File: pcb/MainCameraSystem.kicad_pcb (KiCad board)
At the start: 4 copper layers, 50 x 50 mm, 5 parts, among them J1 OV5640 Ribbon Connector, J2 ST-Link, J3 Micro_SD_Card, U1 STM32H533VET6

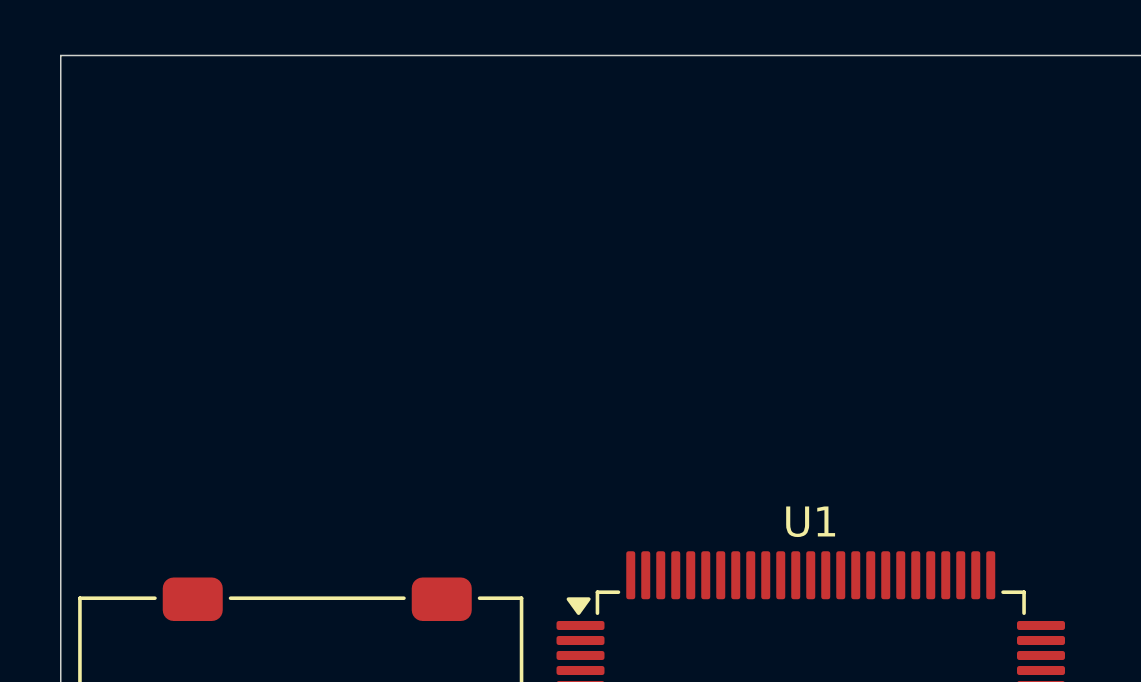
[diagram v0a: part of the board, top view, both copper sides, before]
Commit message: Integrated UART Bridge onto Camera PCB
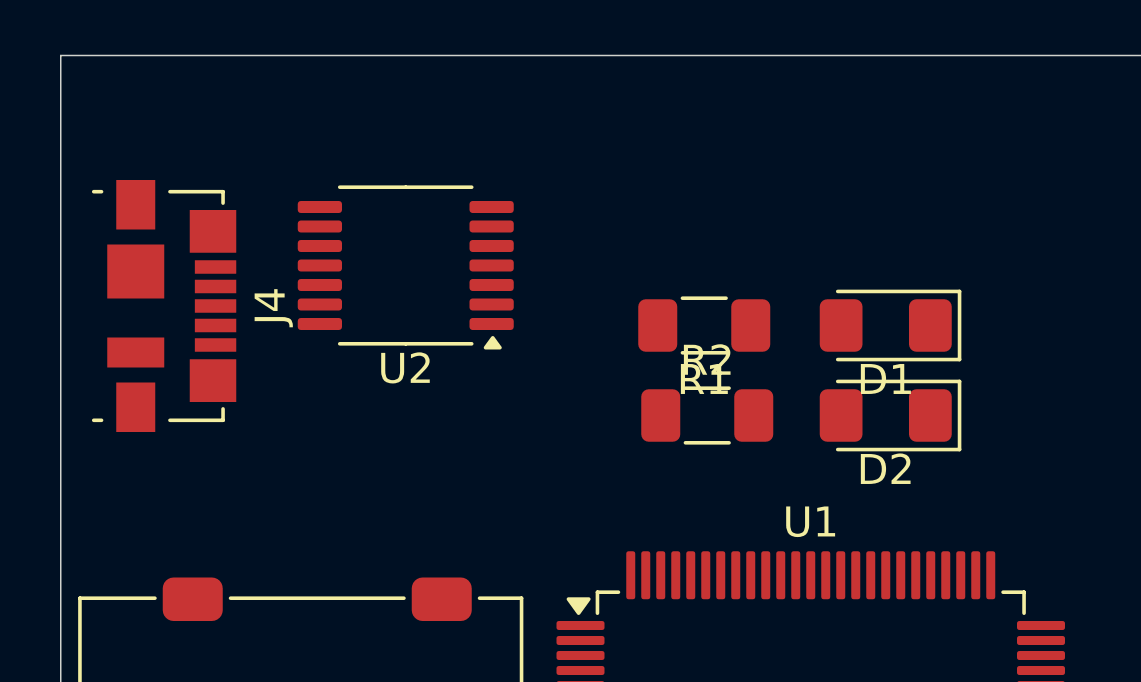
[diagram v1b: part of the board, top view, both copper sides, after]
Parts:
- added D1: GREEN, LED_SMD:LED_1206_3216Metric_Pad1.42x1.75mm_HandSolder, F.Cu at (152.5, 84.0)
- added D2: RED, LED_SMD:LED_1206_3216Metric_Pad1.42x1.75mm_HandSolder, F.Cu at (152.5, 87.0)
- added J4: USB_B_Micro, Connector_USB:USB_Micro-B_Molex_47346-0001, F.Cu at (128.7, 83.3)
- added R1: 2K, Resistor_SMD:R_1206_3216Metric_Pad1.30x1.75mm_HandSolder, F.Cu at (146.4, 84.0)
- added R2: 2K, Resistor_SMD:R_1206_3216Metric_Pad1.30x1.75mm_HandSolder, F.Cu at (146.6, 87.0)
- added U2: MCP2221AxST, Package_SO:TSSOP-14_4.4x5mm_P0.65mm, F.Cu at (136.5, 82.0)

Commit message: Emptied out schematic and layout of `MainCameraSystem`.
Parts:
- removed D1: GREEN, LED_SMD:LED_1206_3216Metric_Pad1.42x1.75mm_HandSolder
- removed D2: RED, LED_SMD:LED_1206_3216Metric_Pad1.42x1.75mm_HandSolder
- removed J1: OV5640 Ribbon Connector, pcb:Flat Flexible Cable 24-Pin 0.5mm Connector
- removed J2: ST-Link, Connector_IDC:IDC-Header_2x05_P2.54mm_Horizontal
- removed J3: Micro_SD_Card, pcb:microSD_HC_Molex_47219-2001
- removed J4: USB_B_Micro, Connector_USB:USB_Micro-B_Molex_47346-0001
- removed N1: Housing, pcb:MainCameraSystemHousing
- removed R1, R2: 2K, Resistor_SMD:R_1206_3216Metric_Pad1.30x1.75mm_HandSolder
- removed U1: STM32H533VET6, Package_QFP:LQFP-100_14x14mm_P0.5mm
- removed U2: MCP2221AxST, Package_SO:TSSOP-14_4.4x5mm_P0.65mm
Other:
- board outline removed

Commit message: Most of the essential components slapped together for `MainCameraSystem`.
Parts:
- added D5: 150141M173100, LED_SMD:LED_RGB_Wuerth-PLCC4_3.2x2.8mm_150141M173100, F.Cu at (133.0, 90.0)
- added H1: MountingHole, MountingHole:MountingHole_3.2mm_M3, F.Cu at (134.0, 84.0)
- added H2: MountingHole, MountingHole:MountingHole_3.2mm_M3, F.Cu at (166.0, 84.0)
- added H3: MountingHole, MountingHole:MountingHole_3.2mm_M3, F.Cu at (134.0, 116.0)
- added H4: MountingHole, MountingHole:MountingHole_3.2mm_M3, F.Cu at (166.0, 116.0)
- added J1: 0472192001, pcb:microSD_HC_Molex_47219-2001, B.Cu at (150.0, 88.0)
- added J2: Debug, pcb:Molex_PicoBlade_53047-1010_1x10_P1.25mm_Vertical, F.Cu at (131.5, 94.4)
- added J6: FFC2B28-24-G, pcb:Flat Flexible Cable 24-Pin 0.5mm Connector, F.Cu at (149.2, 117.0)
- added SW1: B3U-1000P, Button_Switch_SMD:SW_SPST_B3U-1000P, F.Cu at (133.0, 110.0)
- added SW1: B3U-1000P, Button_Switch_SMD:SW_SPST_B3U-1000P, F.Cu at (136.0, 100.0)
- added U1: STM32H533VET6, Package_QFP:LQFP-100_14x14mm_P0.5mm, F.Cu at (150.0, 100.0)
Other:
- board outline added: 40 x 40 mm

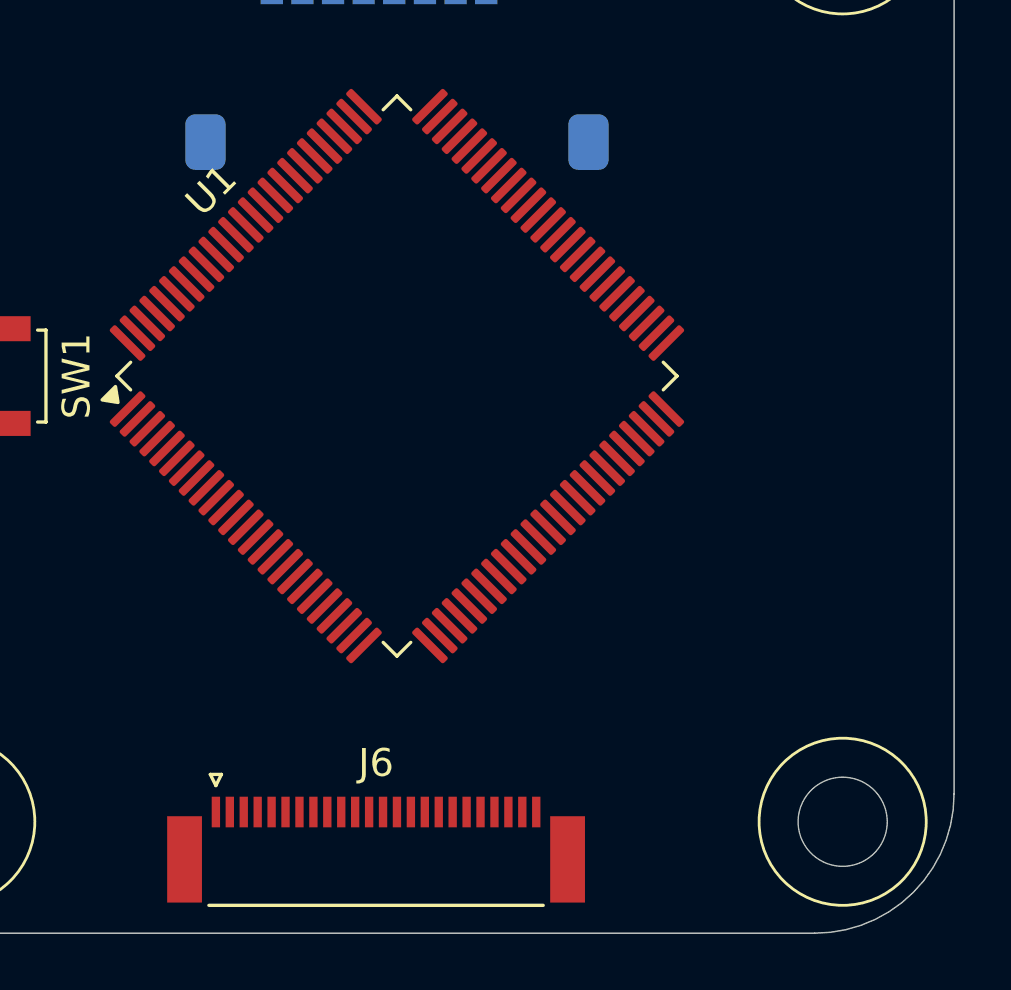
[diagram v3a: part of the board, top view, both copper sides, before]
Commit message: Moved ribbon cable for `MainCameraSystem` per Devon's request.
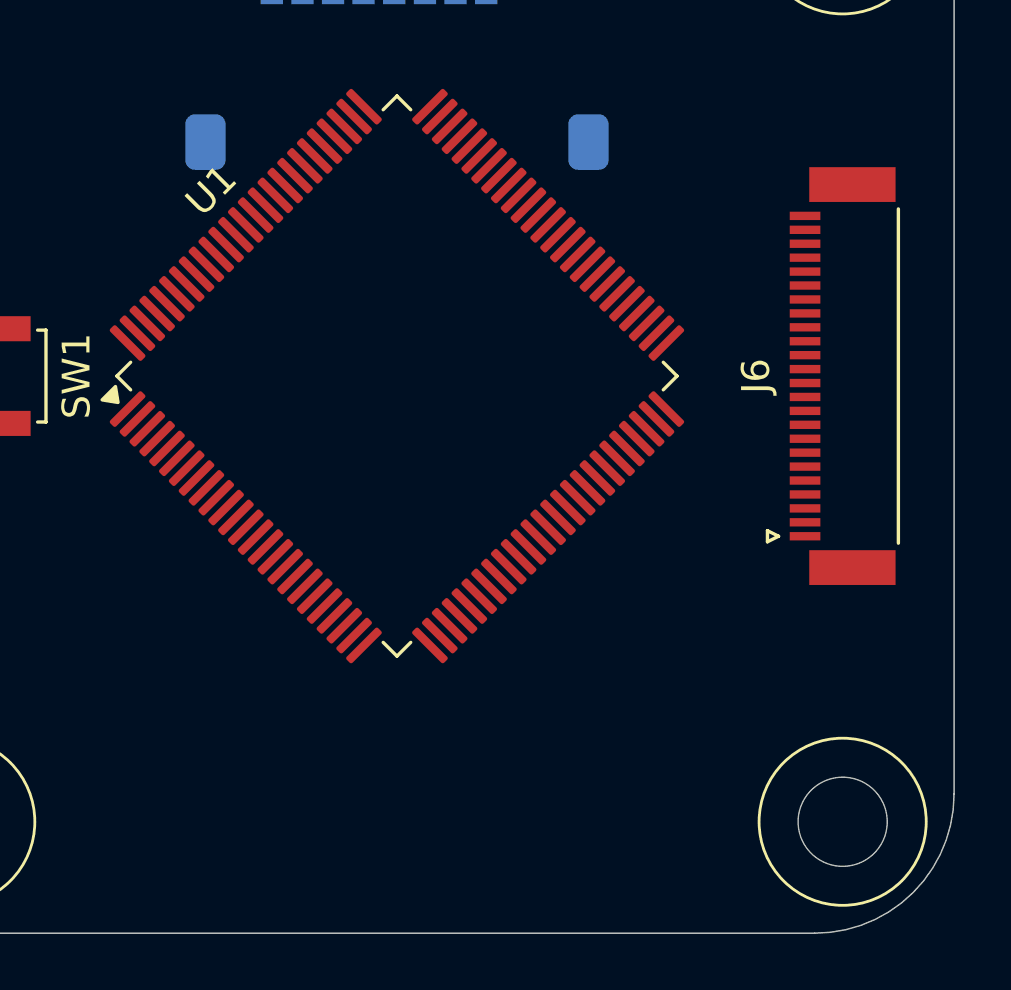
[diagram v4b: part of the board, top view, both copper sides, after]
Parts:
- moved J6 23.9 mm to (166.0, 100.0), turned to 90 degrees
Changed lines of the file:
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@@
 	(footprint "pcb:Flat Flexible Cable 24-Pin 0.5mm Connector"
 		(layer "F.Cu")
-		(at 149.25 117)
+		(at 166 100 90)
 		(descr "FFC/FPC connector, 24 top-side contacts, 0.5mm pitch, SMT")
 		(property "Reference" "J6"
-			(at 0 -3.11 0)
+			(at 0 -3.11 90)
 			(layer "F.SilkS")
 			(effects
@@
 		)
 		(property "Value" "FFC2B28-24-G"
-			(at 0 4.950001 0)
+			(at 0 4.950001 90)
 			(layer "F.Fab")
 			(hide yes)
@@
 		)
 		(property "Datasheet" "~"
-			(at 0 0 0)
+			(at 0 0 90)
 			(layer "F.Fab")
 			(hide yes)
@@
 		)
 		(property "Description" "Generic connector, single row, 01x24, script generated (kicad-library-utils/schlib/autogen/connector/)"
-			(at 0 0 0)
+			(at 0 0 90)
 			(layer "F.Fab")
 			(hide yes)
@@
 		)
 		(property "DigiKey" "https://www.digikey.com/en/products/detail/gct/FFC2B28-24-G/10656928"
-			(at 0 0 0)
+			(at 0 0 90)
 			(layer "F.SilkS")
 			(hide yes)
@@
 		(attr smd)
 		(fp_line
+			(start -5.55 -2.7)
+			(end -5.95 -2.7)
+			(stroke
+				(width 0.12)
+				(type solid)
+			)
+			(layer "F.SilkS")
+		)
+		(fp_line
+			(start -5.95 -2.7)
+			(end -5.75 -2.300001)
+			(stroke
+				(width 0.12)
+				(type solid)
+			)
+			(layer "F.SilkS")
+		)
+		(fp_line
+			(start -5.75 -2.300001)
+			(end -5.55 -2.7)
+			(stroke
+				(width 0.12)
+				(type solid)
+			)
+			(layer "F.SilkS")
+		)
+		(fp_line
 			(start -6 2)
 			(end 6 2)
@@
 			(layer "F.SilkS")
 		)
-		(fp_line
-			(start -5.95 -2.7)
-			(end -5.75 -2.300001)
-			(stroke
-				(width 0.12)
-				(type solid)
-			)
-			(layer "F.SilkS")
-		)
-		(fp_line
-			(start -5.75 -2.300001)
-			(end -5.55 -2.7)
-			(stroke
-				(width 0.12)
-				(type solid)
-			)
-			(layer "F.SilkS")
-		)
-		(fp_line
-			(start -5.55 -2.7)
-			(end -5.95 -2.7)
-			(stroke
-				(width 0.12)
-				(type solid)
-			)
-			(layer "F.SilkS")
-		)
 		(pad "" smd rect
-			(at -6.875 0.349999)
+			(at -6.875 0.349999 90)
 			(size 1.25 3.1)
 			(layers "F.Cu" "F.Mask" "F.Paste")
 		)
 		(pad "" smd rect
-			(at 6.875 0.349999)
+			(at 6.875 0.349999 90)
 			(size 1.25 3.1)
 			(layers "F.Cu" "F.Mask" "F.Paste")
 		)
 		(pad "1" smd rect
-			(at -5.75 -1.35)
+			(at -5.75 -1.35 90)
 			(size 0.3 1.1)
 			(layers "F.Cu" "F.Mask" "F.Paste")
@@
 		)
 		(pad "2" smd rect
-			(at -5.25 -1.35)
+			(at -5.25 -1.35 90)
 			(size 0.3 1.1)
 			(layers "F.Cu" "F.Mask" "F.Paste")
@@
 		)
 		(pad "3" smd rect
-			(at -4.75 -1.35)
+			(at -4.75 -1.35 90)
 			(size 0.3 1.1)
 			(layers "F.Cu" "F.Mask" "F.Paste")
@@
 		)
 		(pad "4" smd rect
-			(at -4.25 -1.35)
+			(at -4.25 -1.35 90)
 			(size 0.3 1.1)
 			(layers "F.Cu" "F.Mask" "F.Paste")
@@
 		)
 		(pad "5" smd rect
-			(at -3.75 -1.35)
+			(at -3.75 -1.35 90)
 			(size 0.3 1.1)
 			(layers "F.Cu" "F.Mask" "F.Paste")
@@
 		)
 		(pad "6" smd rect
-			(at -3.25 -1.35)
+			(at -3.25 -1.35 90)
 			(size 0.3 1.1)
 			(layers "F.Cu" "F.Mask" "F.Paste")
@@
 		)
 		(pad "7" smd rect
-			(at -2.75 -1.35)
+			(at -2.75 -1.35 90)
 			(size 0.3 1.1)
 			(layers "F.Cu" "F.Mask" "F.Paste")
@@
 		)
 		(pad "8" smd rect
-			(at -2.25 -1.35)
+			(at -2.25 -1.35 90)
 			(size 0.3 1.1)
 			(layers "F.Cu" "F.Mask" "F.Paste")
@@
 		)
 		(pad "9" smd rect
-			(at -1.75 -1.35)
+			(at -1.75 -1.35 90)
 			(size 0.3 1.1)
 			(layers "F.Cu" "F.Mask" "F.Paste")
@@
 		)
 		(pad "10" smd rect
-			(at -1.25 -1.35)
+			(at -1.25 -1.35 90)
 			(size 0.3 1.1)
 			(layers "F.Cu" "F.Mask" "F.Paste")
@@
 		)
 		(pad "11" smd rect
-			(at -0.75 -1.35)
+			(at -0.75 -1.35 90)
 			(size 0.3 1.1)
 			(layers "F.Cu" "F.Mask" "F.Paste")
@@
 		)
 		(pad "12" smd rect
-			(at -0.25 -1.35)
+			(at -0.25 -1.35 90)
 			(size 0.3 1.1)
 			(layers "F.Cu" "F.Mask" "F.Paste")
@@
 		)
 		(pad "13" smd rect
-			(at 0.25 -1.35)
+			(at 0.25 -1.35 90)
 			(size 0.3 1.1)
 			(layers "F.Cu" "F.Mask" "F.Paste")
@@
 		)
 		(pad "14" smd rect
-			(at 0.75 -1.35)
+			(at 0.75 -1.35 90)
 			(size 0.3 1.1)
 			(layers "F.Cu" "F.Mask" "F.Paste")
@@
 		)
 		(pad "15" smd rect
-			(at 1.25 -1.35)
+			(at 1.25 -1.35 90)
 			(size 0.3 1.1)
 			(layers "F.Cu" "F.Mask" "F.Paste")
@@
 		)
 		(pad "16" smd rect
-			(at 1.75 -1.35)
+			(at 1.75 -1.35 90)
 			(size 0.3 1.1)
 			(layers "F.Cu" "F.Mask" "F.Paste")
@@
 		)
 		(pad "17" smd rect
-			(at 2.25 -1.35)
+			(at 2.25 -1.35 90)
 			(size 0.3 1.1)
 			(layers "F.Cu" "F.Mask" "F.Paste")
@@
 		)
 		(pad "18" smd rect
-			(at 2.75 -1.35)
+			(at 2.75 -1.35 90)
 			(size 0.3 1.1)
 			(layers "F.Cu" "F.Mask" "F.Paste")
@@
 		)
 		(pad "19" smd rect
-			(at 3.25 -1.35)
+			(at 3.25 -1.35 90)
 			(size 0.3 1.1)
 			(layers "F.Cu" "F.Mask" "F.Paste")
@@
 		)
 		(pad "20" smd rect
-			(at 3.75 -1.35)
+			(at 3.75 -1.35 90)
 			(size 0.3 1.1)
 			(layers "F.Cu" "F.Mask" "F.Paste")
@@
 		)
 		(pad "21" smd rect
-			(at 4.25 -1.35)
+			(at 4.25 -1.35 90)
 			(size 0.3 1.1)
 			(layers "F.Cu" "F.Mask" "F.Paste")
@@
 		)
 		(pad "22" smd rect
-			(at 4.75 -1.35)
+			(at 4.75 -1.35 90)
 			(size 0.3 1.1)
 			(layers "F.Cu" "F.Mask" "F.Paste")
@@
 		)
 		(pad "23" smd rect
-			(at 5.25 -1.35)
+			(at 5.25 -1.35 90)
 			(size 0.3 1.1)
 			(layers "F.Cu" "F.Mask" "F.Paste")
@@
 		)
 		(pad "24" smd rect
-			(at 5.75 -1.35)
-			(size 0.3 1.1)
-			(layers "F.Cu" "F.Mask" "F.Paste")
+			(at 5.75 -1.35 90)
+			(size 0.3 1.1)
+			(layers "F.Cu" "F.Mask" "F.Paste")

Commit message: Laying out some `MainCameraSystem` components; made mirrored FFC ribbon footprint.
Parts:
- removed D5: 150141M173100, LED_SMD:LED_RGB_Wuerth-PLCC4_3.2x2.8mm_150141M173100
- removed J6: FFC2B28-24-G, pcb:Flat Flexible Cable 24-Pin 0.5mm Connector
- removed the SW1 at (133.0, 110.0)
- removed the SW1 at (136.0, 100.0)
- added C1: 100n, Capacitor_SMD:C_1206_3216Metric_Pad1.33x1.80mm_HandSolder, F.Cu at (75.2, 69.7)
- added C10: 1u, Capacitor_SMD:C_1206_3216Metric_Pad1.33x1.80mm_HandSolder, F.Cu at (81.3, 73.0)
- added C11: 1u, Capacitor_SMD:C_1206_3216Metric_Pad1.33x1.80mm_HandSolder, F.Cu at (81.3, 76.4)
- added C12: 100n, Capacitor_SMD:C_1206_3216Metric_Pad1.33x1.80mm_HandSolder, F.Cu at (81.3, 79.7)
- added C13: 100n, Capacitor_SMD:C_1206_3216Metric_Pad1.33x1.80mm_HandSolder, F.Cu at (81.3, 83.1)
- added C14: 10u, Capacitor_SMD:C_1206_3216Metric_Pad1.33x1.80mm_HandSolder, F.Cu at (81.3, 86.4)
- added C15: 10u, Capacitor_SMD:C_1206_3216Metric_Pad1.33x1.80mm_HandSolder, F.Cu at (81.3, 89.8)
- added C16: 100n, Capacitor_SMD:C_1206_3216Metric_Pad1.33x1.80mm_HandSolder, F.Cu at (81.3, 93.1)
- added C17: 100n, Capacitor_SMD:C_1206_3216Metric_Pad1.33x1.80mm_HandSolder, F.Cu at (87.3, 69.7)
- added C18: 10u, Capacitor_SMD:C_1206_3216Metric_Pad1.33x1.80mm_HandSolder, F.Cu at (87.3, 73.0)
- added C19: 10u, Capacitor_SMD:C_1206_3216Metric_Pad1.33x1.80mm_HandSolder, F.Cu at (87.3, 76.4)
- added C2: 22p, Capacitor_SMD:C_1206_3216Metric_Pad1.33x1.80mm_HandSolder, F.Cu at (75.2, 73.0)
- added C20: 100n, Capacitor_SMD:C_1206_3216Metric_Pad1.33x1.80mm_HandSolder, F.Cu at (87.3, 79.7)
- added C21: 100n, Capacitor_SMD:C_1206_3216Metric_Pad1.33x1.80mm_HandSolder, F.Cu at (87.3, 83.1)
- added C22: 2u2, Capacitor_SMD:C_1206_3216Metric_Pad1.33x1.80mm_HandSolder, F.Cu at (87.3, 86.4)
- added C23: 2u2, Capacitor_SMD:C_1206_3216Metric_Pad1.33x1.80mm_HandSolder, F.Cu at (87.3, 89.8)
- added C24: 1u, Capacitor_SMD:C_1206_3216Metric_Pad1.33x1.80mm_HandSolder, F.Cu at (81.2, 126.1)
- added C25: 100n, Capacitor_SMD:C_1206_3216Metric_Pad1.33x1.80mm_HandSolder, F.Cu at (81.2, 129.4)
- added C26: 10n, Capacitor_SMD:C_1206_3216Metric_Pad1.33x1.80mm_HandSolder, F.Cu at (81.2, 132.8)
- added C3: 10u, Capacitor_SMD:C_1206_3216Metric_Pad1.33x1.80mm_HandSolder, F.Cu at (75.2, 76.4)
- added C4: 10u, Capacitor_SMD:C_1206_3216Metric_Pad1.33x1.80mm_HandSolder, F.Cu at (75.2, 79.7)
- added C5: 10n, Capacitor_SMD:C_1206_3216Metric_Pad1.33x1.80mm_HandSolder, F.Cu at (75.2, 83.1)
- added C6: 10u, Capacitor_SMD:C_1206_3216Metric_Pad1.33x1.80mm_HandSolder, F.Cu at (75.2, 86.4)
- added C7: 1u, Capacitor_SMD:C_1206_3216Metric_Pad1.33x1.80mm_HandSolder, F.Cu at (75.2, 89.8)
- added C8: 4u7, Capacitor_SMD:C_1206_3216Metric_Pad1.33x1.80mm_HandSolder, F.Cu at (75.2, 93.1)
- added C9: 100n, Capacitor_SMD:C_1206_3216Metric_Pad1.33x1.80mm_HandSolder, F.Cu at (81.3, 69.7)
- added D1: 150141M173100, LED_SMD:LED_RGB_Wuerth-PLCC4_3.2x2.8mm_150141M173100, F.Cu at (111.1, 77.8)
- added FB1: Ferrite, Inductor_SMD:L_1206_3216Metric_Pad1.42x1.75mm_HandSolder, F.Cu at (93.2, 69.6)
- added J3: 0472192001, pcb:microSD_HC_Molex_47219-2001, B.Cu at (162.2, 100.0)
- added R1: 10k, Resistor_SMD:R_1206_3216Metric_Pad1.30x1.75mm_HandSolder, F.Cu at (93.2, 73.0)
- added R10: 1K, Resistor_SMD:R_1206_3216Metric_Pad1.30x1.75mm_HandSolder, F.Cu at (99.2, 82.9)
- added R11: R_Small, Resistor_SMD:R_1206_3216Metric_Pad1.30x1.75mm_HandSolder, F.Cu at (75.2, 110.0)
- added R12: R_Small, Resistor_SMD:R_1206_3216Metric_Pad1.30x1.75mm_HandSolder, F.Cu at (75.2, 113.3)
- added R13: R_Small, Resistor_SMD:R_1206_3216Metric_Pad1.30x1.75mm_HandSolder, F.Cu at (75.2, 116.6)
- added R14: R_Small, Resistor_SMD:R_1206_3216Metric_Pad1.30x1.75mm_HandSolder, F.Cu at (75.2, 119.9)
- added R15: R_Small, Resistor_SMD:R_1206_3216Metric_Pad1.30x1.75mm_HandSolder, F.Cu at (75.2, 123.2)
- added R16: R_Small, Resistor_SMD:R_1206_3216Metric_Pad1.30x1.75mm_HandSolder, F.Cu at (75.2, 126.6)
- added R2: 10k, Resistor_SMD:R_1206_3216Metric_Pad1.30x1.75mm_HandSolder, F.Cu at (93.2, 76.3)
- added R3: 10k, Resistor_SMD:R_1206_3216Metric_Pad1.30x1.75mm_HandSolder, F.Cu at (93.2, 79.6)
- added R4: 10k, Resistor_SMD:R_1206_3216Metric_Pad1.30x1.75mm_HandSolder, F.Cu at (93.2, 82.9)
- added R5: 47k, Resistor_SMD:R_1206_3216Metric_Pad1.30x1.75mm_HandSolder, F.Cu at (93.2, 86.2)
- added R6: 2K, Resistor_SMD:R_1206_3216Metric_Pad1.30x1.75mm_HandSolder, F.Cu at (99.2, 69.6)
- added R7: 100, Resistor_SMD:R_1206_3216Metric_Pad1.30x1.75mm_HandSolder, F.Cu at (99.2, 73.0)
- added R8: 2K, Resistor_SMD:R_1206_3216Metric_Pad1.30x1.75mm_HandSolder, F.Cu at (99.2, 76.3)
- added R9: 2K, Resistor_SMD:R_1206_3216Metric_Pad1.30x1.75mm_HandSolder, F.Cu at (99.2, 79.6)
- added SW1: B3U-1000P, Button_Switch_SMD:SW_SPST_B3U-1000P, F.Cu at (105.1, 77.8)
- added SW2: B3U-1000P, Button_Switch_SMD:SW_SPST_B3U-1000P, F.Cu at (105.1, 82.1)
- added U2: TLV70028DDCR, Package_TO_SOT_SMD:SOT-353_SC-70-5, F.Cu at (110.9, 89.8)
- added U3: TLV70015DDCR, Package_TO_SOT_SMD:SOT-23-5, F.Cu at (110.6, 82.3)
- added Y1: ASV-24.000MHZ-EJ-T, Oscillator:Oscillator_SMD_Abracon_ASV-4Pin_7.0x5.1mm, F.Cu at (105.8, 122.3)
- J1: value 0472192001 -> FFC2B28-24-G; footprint pcb:microSD_HC_Molex_47219-2001 -> pcb:Flat Flexible Cable 24-Pin 0.5mm Connector - REVERSED; moved to F.Cu
- moved J1 29.4 mm to (150.0, 117.4), turned to 0 degrees
- moved J2 17.2 mm to (144.4, 82.9), turned to 0 degrees
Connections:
- J1 pad 1: Net-(J1-DAT2) -> unconnected-(J1-Pin_1-Pad1)
- J1 pad 2: Net-(J1-DAT3/CD) -> GNDA
- J1 pad 3: Net-(J1-CMD) -> ovcam_i2c_data
- J1 pad 4: +3.3V -> +2V8
- J1 pad 5: Net-(J1-CLK) -> ovcam_i2c_clock
- J1 pad 6: GND -> ovcam_reset
- J1 pad 7: Net-(J1-DAT0) -> ovcam_vsync
- J1 pad 8: Net-(J1-DAT1) -> ovcam_power_down
- J1 pad 9: GND -> ovcam_hsync
- U1 pad 1: unconnected-(U1-PE2-Pad1) -> ovcam_y5
- U1 pad 10: Net-(U1-VSS-Pad10) -> GND
- U1 pad 100: unconnected-(U1-VDD-Pad100) -> +3.3V
- U1 pad 11: unconnected-(U1-VDD-Pad11) -> +3.3V
- U1 pad 14: unconnected-(U1-NRST-Pad14) -> RESET
- U1 pad 16: unconnected-(U1-PC1-Pad16) -> led_channel_green
- U1 pad 19: unconnected-(U1-VSSA-Pad19) -> GND
- U1 pad 2: unconnected-(U1-PE3-Pad2) -> led_channel_blue
- U1 pad 20: unconnected-(U1-VREF--Pad20) -> GND
- U1 pad 21: unconnected-(U1-VREF+-Pad21) -> +3.3V
- U1 pad 22: unconnected-(U1-VDDA-Pad22) -> +3.3V
- U1 pad 25: unconnected-(U1-PA2-Pad25) -> stlink_tx
- U1 pad 26: unconnected-(U1-PA3-Pad26) -> stlink_rx
- U1 pad 27: Net-(U1-VSS-Pad10) -> GND
- U1 pad 28: unconnected-(U1-VDD-Pad28) -> +3.3V
- U1 pad 29: unconnected-(U1-PA4-Pad29) -> ovcam_hsync
- U1 pad 3: unconnected-(U1-PE4-Pad3) -> ovcam_y6
- U1 pad 31: unconnected-(U1-PA6-Pad31) -> ovcam_pixel_clock
- U1 pad 4: unconnected-(U1-PE5-Pad4) -> ovcam_power_down
- U1 pad 47: unconnected-(U1-PB10-Pad47) -> ovcam_i2c_clock
- U1 pad 48: unconnected-(U1-VCAP-Pad48) -> VCAP
- U1 pad 49: Net-(U1-VSS-Pad10) -> GND
- U1 pad 5: unconnected-(U1-PE6-Pad5) -> ovcam_reset
- U1 pad 50: unconnected-(U1-VDD-Pad50) -> +3.3V
- U1 pad 51: unconnected-(U1-PB12-Pad51) -> ovcam_i2c_data
- U1 pad 54: unconnected-(U1-PB15-Pad54) -> ovcam_y4
- U1 pad 6: unconnected-(U1-VBAT-Pad6) -> +3.3V
- U1 pad 63: unconnected-(U1-PC6-Pad63) -> ovcam_y2
- U1 pad 64: unconnected-(U1-PC7-Pad64) -> ovcam_y3
- U1 pad 65: unconnected-(U1-PC8-Pad65) -> sd_data_0
- U1 pad 66: unconnected-(U1-PC9-Pad66) -> sd_data_1
- U1 pad 72: unconnected-(U1-PA13(JTMS-Pad72) -> swdio
- U1 pad 73: unconnected-(U1-VDDUSB-Pad73) -> +3.3V
- U1 pad 74: Net-(U1-VSS-Pad10) -> GND
- U1 pad 75: unconnected-(U1-VDD-Pad75) -> +3.3V
- U1 pad 76: unconnected-(U1-PA14(JTCK-Pad76) -> swclk
- U1 pad 78: unconnected-(U1-PC10-Pad78) -> sd_data_2
- U1 pad 79: unconnected-(U1-PC11-Pad79) -> sd_data_3
- U1 pad 80: unconnected-(U1-PC12-Pad80) -> sd_clock
- U1 pad 83: unconnected-(U1-PD2-Pad83) -> sd_cmd
- U1 pad 89: unconnected-(U1-PB3(JTDO-Pad89) -> swo
- U1 pad 90: unconnected-(U1-PB4(NJTRST)-Pad90) -> ovcam_y9
- U1 pad 92: unconnected-(U1-PB6-Pad92) -> ovcam_y7
- U1 pad 93: unconnected-(U1-PB7-Pad93) -> ovcam_vsync
- U1 pad 94: unconnected-(U1-BOOT0-Pad94) -> BOOT0
- U1 pad 95: unconnected-(U1-PB8-Pad95) -> ovcam_y8
- U1 pad 97: unconnected-(U1-PE0-Pad97) -> led_channel_red
- U1 pad 98: unconnected-(U1-VCAP-Pad98) -> VCAP
- U1 pad 99: Net-(U1-VSS-Pad10) -> GND
